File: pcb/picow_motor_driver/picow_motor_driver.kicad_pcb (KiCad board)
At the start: 2 copper layers, 68 x 35 mm, 21 parts, among them J1 Conn_01x02_Pin, J2 Conn_01x05_Pin, J3 Conn_01x04_Pin, U1 Pico

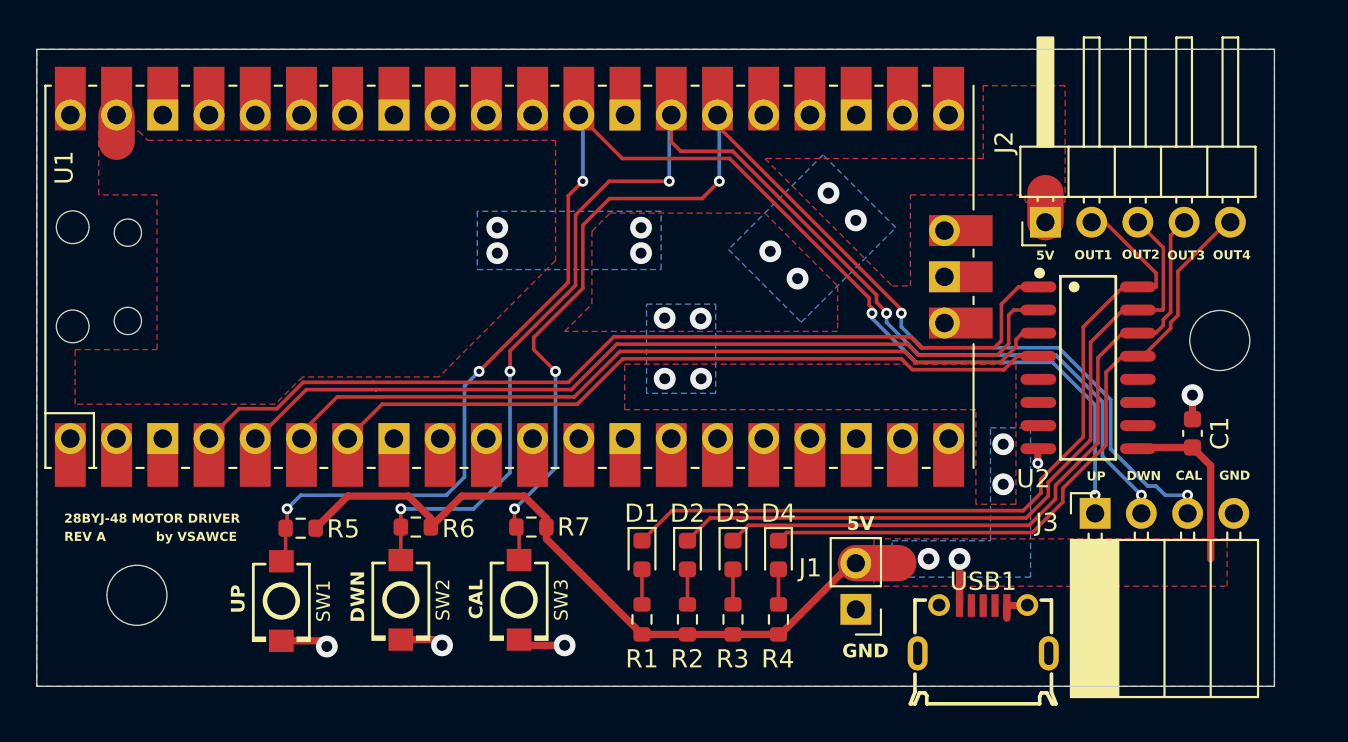
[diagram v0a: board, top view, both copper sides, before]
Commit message: Changed connectors out to JST, switched USB conn
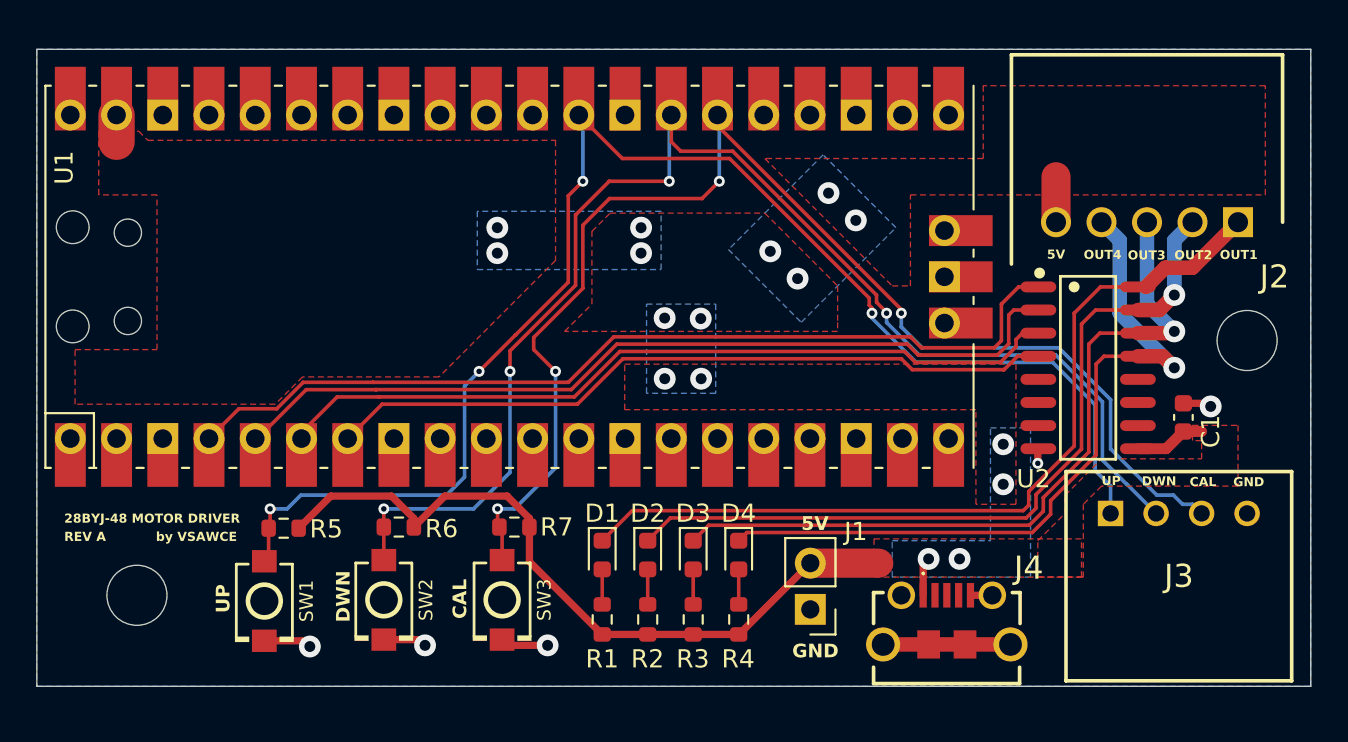
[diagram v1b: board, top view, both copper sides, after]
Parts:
- removed USB1: ~, Library:MICRO-USB-SMD_5P-P0.65-H-F_C10418
- added J4: 10118194-0001LF, Library:101181940001LF, F.Cu at (152.0, 97.3)
- J2: footprint Connector_PinHeader_2.54mm:PinHeader_1x05_P2.54mm_Horizontal -> Library:S5B-XH-A
- J3: footprint Connector_PinSocket_2.54mm:PinSocket_1x04_P2.54mm_Horizontal -> Library:S4BXHALFSN
- moved J2 10.6 mm to (168.0, 74.5), turned to 0 degrees
- moved J1 2.50 mm to (144.5, 95.8)
- moved D1 2.19 mm to (133.1, 92.8)
- moved D2 2.19 mm to (135.6, 92.8)
- moved D3 2.19 mm to (138.1, 92.8)
- moved D4 2.19 mm to (140.6, 92.8)
- moved R1 2.19 mm to (133.1, 96.3)
- moved R2 2.19 mm to (135.6, 96.3)
- moved R3 2.19 mm to (138.1, 96.3)
- moved R4 2.19 mm to (140.6, 96.3)
- moved C1 1.01 mm to (165.0, 85.2)
- moved R5 0.94 mm to (115.6, 91.3)
- moved R6 0.94 mm to (121.9, 91.2)
- moved R7 0.94 mm to (128.2, 91.2)
- moved SW1 0.94 mm to (114.5, 95.3)
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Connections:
- J2 pad 1: +5V -> Net-(D1-K)
- J2 pad 2: Net-(D1-K) -> Net-(D2-K)
- J2 pad 3: Net-(D2-K) -> Net-(D3-K)
- J2 pad 4: Net-(D3-K) -> Net-(D4-K)
- J2 pad 5: Net-(D4-K) -> +5V
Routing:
- net GND: track 13.3 -> 19.1 mm
- net Net-(D4-K): track 36.8 -> 41.7 mm, vias 0 -> 1
- net +5V: track 55.2 -> 50.9 mm
- net Net-(D3-K): track 37.9 -> 40.9 mm, vias 0 -> 1
- net Net-(D1-K): track 43.5 -> 46.1 mm
- net Net-(D2-K): track 40.4 -> 42.6 mm, vias 0 -> 1
- net /BUT_DOWN: track 73.5 -> 74.8 mm, vias 5 -> 4
- net /BUT_UP: track 78.0 -> 79.2 mm, vias 5 -> 4
- net /BUT_CAL: track 71.2 -> 72.3 mm, vias 5 -> 4
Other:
- board size 68 x 35 mm -> 70 x 35 mm
